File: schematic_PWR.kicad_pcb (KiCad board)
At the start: 2 copper layers, 100 x 100 mm, 116 parts, among them J1 Conn_01x02, J10 Conn_01x02, J11 Conn_01x02, J12 Conn_01x02, J13 Conn_01x02, J14 Conn_01x02, J2 Conn_01x04, J3 Conn_01x04, J4 STlink_v3, J5 Conn_01x02, J6 Conn_01x02, J7 Conn_01x02, J8 Conn_01x02, J9 Conn_01x02, K1 HE1AN-W-DC12V-Y6, Q1 Q_PMOS_GSD, Q2 Q_PMOS_GSD, Q3 Q_PMOS_GSD, Q4 Q_PMOS_GSD, Q5 Q_NMOS_GSD, Q6 Q_NMOS_GSD, Q7 Q_PMOS_GSD, Q8 Q_NMOS_GSD, SW1 SW_SPST, SW2 SW_SPST, SW3 SW_SPST, U1 MCP2562-H-SN, U2 XR76208, U3 STM32F103CBTx, U4 TPS5430DDA, U5 XC6206P332MR-G, Y1 12MHz

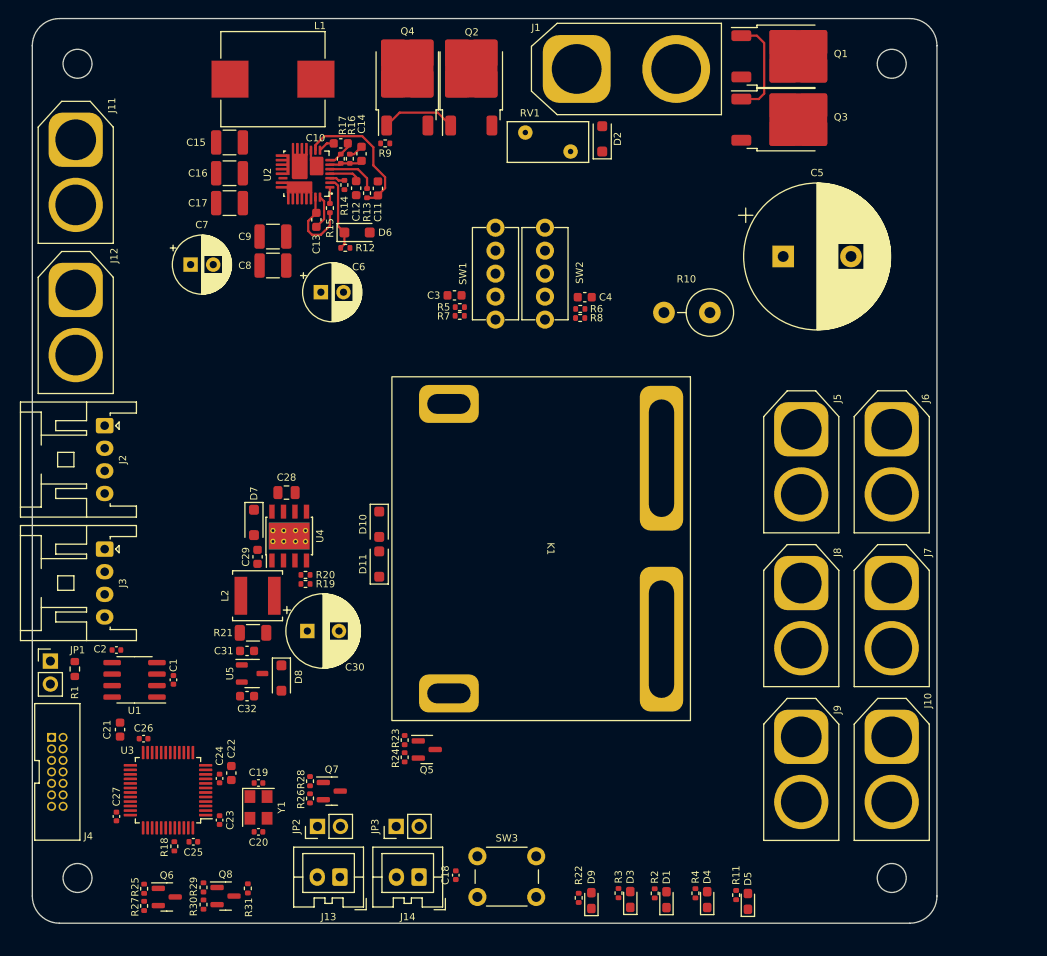
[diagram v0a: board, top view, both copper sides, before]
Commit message: add voltage detector
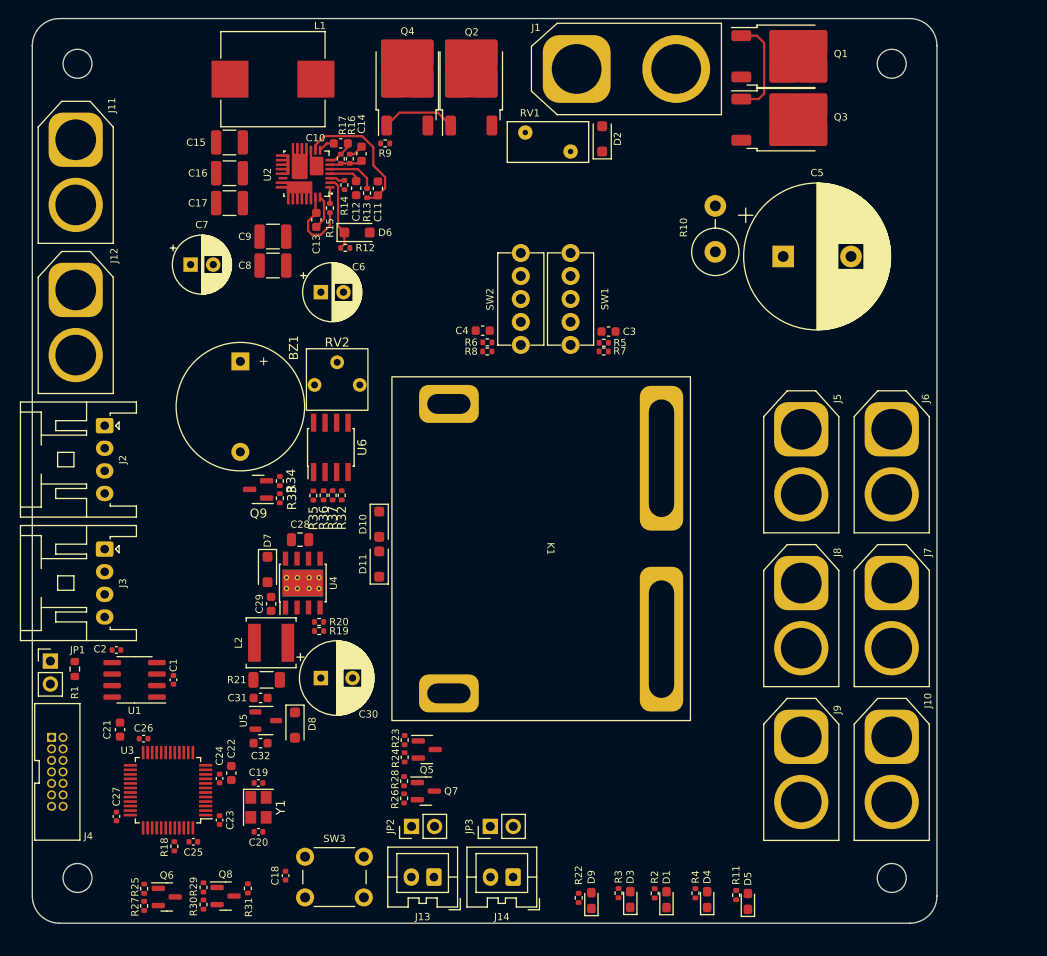
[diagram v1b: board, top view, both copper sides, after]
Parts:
- added BZ1: Buzzer, Buzzer_Beeper:Buzzer_D14mm_H7mm_P10mm, F.Cu at (123.0, 87.9)
- added Q9: Q_NMOS_GSD, Package_TO_SOT_SMD:SOT-23, F.Cu at (125.0, 102.0)
- added R32: R_Small, Resistor_SMD:R_0402_1005Metric, F.Cu at (134.2, 102.7)
- added R33: 100, Resistor_SMD:R_0402_1005Metric, F.Cu at (127.4, 103.0)
- added R34: 10k, Resistor_SMD:R_0402_1005Metric, F.Cu at (127.4, 101.1)
- added R35: 10k, Resistor_SMD:R_0402_1005Metric, F.Cu at (131.1, 102.7)
- added R36: 10k, Resistor_SMD:R_0402_1005Metric, F.Cu at (132.2, 102.7)
- added R37: 20k, Resistor_SMD:R_0402_1005Metric, F.Cu at (133.2, 102.7)
- added RV2: 10k, RDC_generic:GF063P, F.Cu at (133.7, 89.9)
- added U6: LM393, Package_SO:PowerIntegrations_SO-8, F.Cu at (133.0, 97.4)
- C19, C20: value 10pF -> 15pF
- Y1: footprint Crystal:Crystal_SMD_SeikoEpson_FA238V-4Pin_3.2x2.5mm -> Crystal:Crystal_SMD_3225-4Pin_3.2x2.5mm
- moved SW3 19.1 mm to (130.2, 142.7)
- moved C18 18.8 mm to (128.0, 144.7)
- moved C3 17.5 mm to (163.7, 84.6), turned to 180 degrees
- moved R5 16.4 mm to (163.2, 85.8), turned to 180 degrees
- moved R7 16.4 mm to (163.2, 86.8), turned to 0 degrees
- moved C4 11.9 mm to (149.8, 84.5)
- moved R8 10.9 mm to (150.3, 86.8)
- moved R6 10.9 mm to (150.3, 85.8)
- moved J13 10.4 mm to (144.4, 144.9)
- moved J14 10.4 mm to (153.2, 144.9)
- moved JP2 10.4 mm to (141.9, 139.3)
- moved JP3 10.4 mm to (150.6, 139.3)
- moved Q7 10.4 mm to (143.5, 135.4)
- moved R26 10.4 mm to (141.1, 136.2)
- moved R28 10.4 mm to (141.1, 134.3)
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
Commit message: update art work
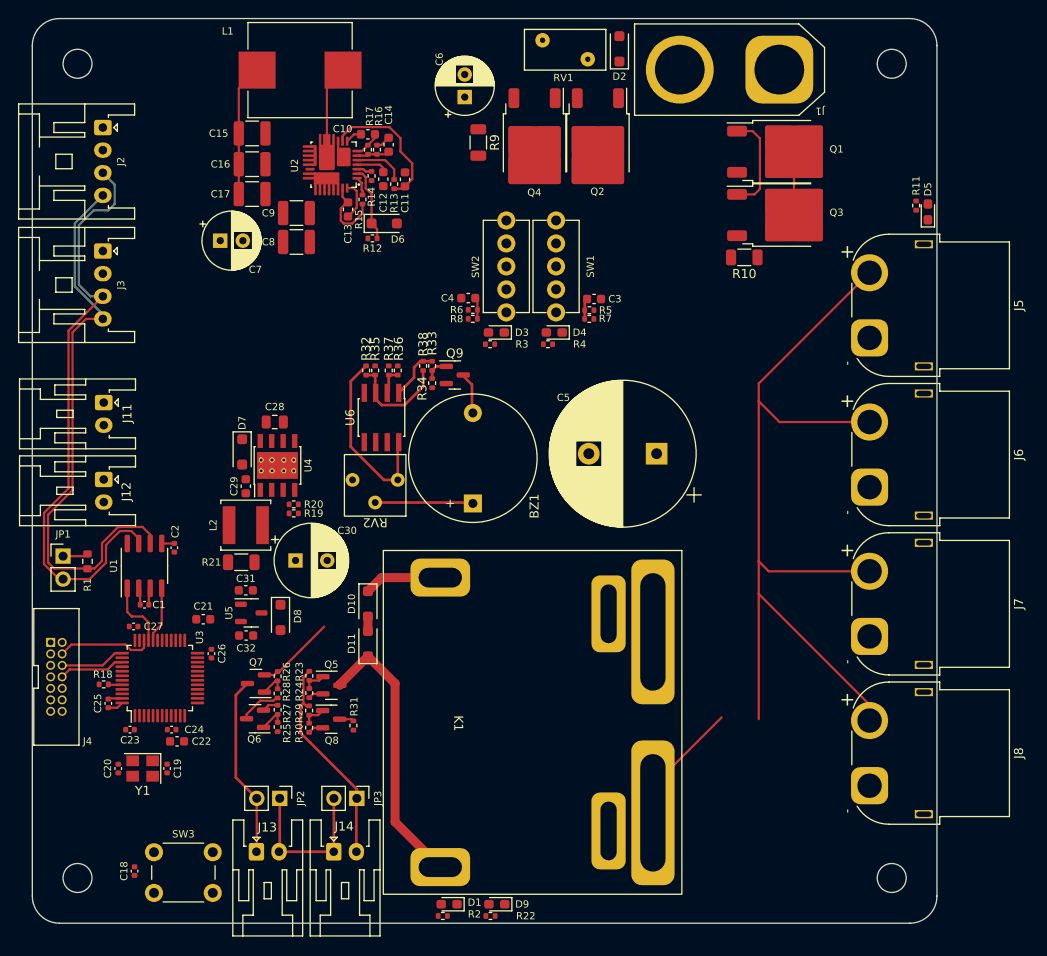
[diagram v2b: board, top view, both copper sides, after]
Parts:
- removed J10, J9: Conn_01x02, Connector_AMASS:AMASS_XT60-F_1x02_P7.20mm_Vertical
- added R38: 15k, Resistor_SMD:R_0402_1005Metric, F.Cu at (143.2, 88.4)
- J11, J12: footprint Connector_AMASS:AMASS_XT60-F_1x02_P7.20mm_Vertical -> Connector_JST:JST_XA_S02B-XASK-1_1x02_P2.50mm_Horizontal
- J13, J14: footprint Connector_JST:JST_XA_B02B-XASK-1_1x02_P2.50mm_Vertical -> Connector_JST:JST_XA_S02B-XASK-1_1x02_P2.50mm_Horizontal
- J5, J6, J7, J8: footprint Connector_AMASS:AMASS_XT60-F_1x02_P7.20mm_Vertical -> Connector_AMASS:AMASS_XT60PW-F_1x02_P7.20mm_Horizontal
- K1: footprint RDC_generic:HE1AN-W-DC12V-Y6 -> RDC_generic:HE1AN-W-DC12V-Y6+Y5
- R10: footprint Resistor_THT:R_Axial_DIN0516_L15.5mm_D5.0mm_P5.08mm_Vertical -> Resistor_SMD:R_1206_3216Metric
- R32: value R_Small -> 2k
- R36: value 10k -> 12K
- R9: footprint Resistor_SMD:R_0402_1005Metric -> Resistor_SMD:R_1206_3216Metric
- moved D5 78.8 mm to (199.0, 71.4)
- moved R11 78.8 mm to (197.7, 70.7)
- moved D4 64.9 mm to (157.7, 84.7), turned to 180 degrees
- moved D3 64.4 mm to (151.3, 84.7), turned to 180 degrees
- moved R4 62.8 mm to (157.0, 86.0), turned to 180 degrees
- moved R3 62.3 mm to (150.6, 86.0), turned to 180 degrees
- moved J2 33.0 mm to (107.8, 62.0)
- moved J3 33.0 mm to (107.8, 75.7)
- moved BZ1 30.1 mm to (148.7, 103.6), turned to 90 degrees
- moved J11 29.2 mm to (107.9, 92.5)
- moved C6 26.8 mm to (147.8, 58.7), turned to 90 degrees
- moved R27 26.2 mm to (127.1, 126.4), turned to 90 degrees
- moved C5 25.9 mm to (169.0, 98.1), turned to 180 degrees
- moved Q9 25.2 mm to (146.7, 89.4), turned to 0 degrees
- moved D1 24.0 mm to (146.1, 147.9), turned to 180 degrees
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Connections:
- Q9 pad 2: /Voltage_detector/GND -> GND
- R32 pad 1: /Voltage_detector/V+ -> +12V
- R32 pad 2: Net-(D12-K) -> Net-(U6A-+)
- R34 pad 1: Net-(Q9-G) -> GND
- R34 pad 2: /Voltage_detector/GND -> Net-(Q9-G)
- R35 pad 1: /Voltage_detector/Vcc -> Net-(U6A-+)
- R35 pad 2: Net-(R33-Pad2) -> GND
- R36 pad 1: /Voltage_detector/V- -> Logic_line_Power
- R37 pad 2: /Voltage_detector/GND -> GND
- RV2 pad 1: /Voltage_detector/Vcc -> +12V
- RV2 pad 3: /Voltage_detector/GND -> GND
- U6 pad 3: Net-(D12-K) -> Net-(U6A-+)
- U6 pad 4: /Voltage_detector/GND -> GND
- U6 pad 8: /Voltage_detector/Vcc -> +12V
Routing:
- net /Power_relay/Main_power_OUT: track 0.00 -> 109.4 mm
- net Net-(J2-Pin_3): track 0.00 -> 66.4 mm
- net Net-(J2-Pin_4): track 0.00 -> 62.7 mm
- net +12V: track 1.63 -> 54.3 mm
- net Net-(D11-K): track 0.00 -> 31.9 mm
- net /EMS/Relay_Signal_OUT: track 0.00 -> 23.7 mm
- net Net-(J13-Pin_1): track 0.00 -> 20.2 mm
- net Net-(J13-Pin_2): track 0.00 -> 17.9 mm
- net Net-(U6A-+): track 0.00 -> 11.8 mm
- net Net-(BZ1--): track 0.00 -> 10.7 mm
- net /STM32F103/SWDIO: track 0.00 -> 10.6 mm
- net Net-(C13-Pad1): track 8.50 -> 18.5 mm
- net GND: track 0.00 -> 8.63 mm
- net /STM32F103/CAN_TX: track 0.00 -> 7.44 mm
- net /STM32F103/SWO: track 0.00 -> 7.31 mm
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
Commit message: アートワークのほとんど終わり
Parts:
- removed C2: 0.1uF, Capacitor_SMD:C_0402_1005Metric
- added R39: 10k, Resistor_SMD:R_1206_3216Metric, F.Cu at (122.5, 83.5)
- D1: footprint LED_SMD:LED_0603_1608Metric_Pad1.05x0.95mm_HandSolder -> LED_SMD:LED_0805_2012Metric
- D10: value D_Schottky -> D
- D11: footprint Diode_SMD:D_SOD-123F -> Diode_SMD:D_SMA
- D2: value D -> D_Schottky
- D3, D4, D5, D9: footprint LED_SMD:LED_0603_1608Metric_Pad1.05x0.95mm_HandSolder -> LED_SMD:LED_0603_1608Metric
- D6: footprint Diode_SMD:D_SOD-123F -> Diode_SMD:D_SOD-123
- L1: value 8.2u -> 8.2uH
- R16: value 38k -> 47k
- R17, R32: value 2k -> 2.4k
- R2: value 10k -> 1.2k
- R36: value 12K -> 12k
- SW3: footprint Button_Switch_THT:SW_PUSH_6mm_H7.3mm -> RDC_generic:TVBP06-B043
- U1: value MCP2562-H-SN -> SN65HVD230
- moved D1 34.7 mm to (111.4, 145.7)
- moved R2 34.7 mm to (110.7, 147.3), turned to 0 degrees
- moved R22 34.0 mm to (116.7, 147.3), turned to 0 degrees
- moved D9 34.0 mm to (117.4, 146.0)
- moved C4 27.6 mm to (165.4, 59.3), turned to -90 degrees
- moved R8 26.7 mm to (164.6, 61.8), turned to -90 degrees
- moved R6 26.5 mm to (165.6, 61.8), turned to 90 degrees
- moved R5 21.4 mm to (178.6, 69.2), turned to -90 degrees
- moved R7 20.6 mm to (177.1, 69.7), turned to 180 degrees
- moved C3 19.1 mm to (176.6, 68.5), turned to 0 degrees
- moved R31 15.4 mm to (133.3, 112.9), turned to 0 degrees
- moved SW3 13.4 mm to (104.0, 132.7), turned to -90 degrees
- moved Q8 12.3 mm to (132.4, 115.1)
- moved R29 12.3 mm to (129.9, 114.2)
- moved R30 12.3 mm to (129.9, 116.1)
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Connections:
- C1 pad 2: +5V -> +3.3V
- C10 pad 2: /Stepdown_12V_8A/GND -> GND
- C11 pad 2: /Stepdown_12V_8A/GND -> GND
- C12 pad 2: /Stepdown_12V_8A/GND -> GND
- C15 pad 2: /Stepdown_12V_8A/GND -> GND
- C16 pad 2: /Stepdown_12V_8A/GND -> GND
- C17 pad 2: /Stepdown_12V_8A/GND -> GND
- C8 pad 2: /Stepdown_12V_8A/GND -> GND
- C9 pad 2: /Stepdown_12V_8A/GND -> GND
- D6 pad 2: /Stepdown_12V_8A/GND -> GND
- R14 pad 2: /Stepdown_12V_8A/GND -> GND
- R17 pad 2: /Stepdown_12V_8A/GND -> GND
- U1 pad 3: +5V -> +3.3V
- U1 pad 5: +3.3V -> unconnected-(U1-Vref-Pad5)
- U2 pad 10: /Stepdown_12V_8A/GND -> GND
- U2 pad 15: /Stepdown_12V_8A/GND -> GND
- U2 pad 16: /Stepdown_12V_8A/GND -> GND
- U2 pad 17: /Stepdown_12V_8A/GND -> GND
- U2 pad 18: /Stepdown_12V_8A/GND -> GND
- U2 pad 19: /Stepdown_12V_8A/GND -> GND
- U2 pad 20: Net-(C13-Pad1) -> unconnected-(U2-SW-Pad20)
- U2 pad 7: /Stepdown_12V_8A/GND -> GND
- U2 pad AGND: /Stepdown_12V_8A/GND -> GND
- U2 pad PGND: /Stepdown_12V_8A/GND -> GND
- U3 pad 17: unconnected-(U3-PA7-Pad17) -> MCU_running
- U3 pad 18: unconnected-(U3-PB0-Pad18) -> /EMS/MCU_EMC_signal
- U3 pad 19: unconnected-(U3-PB1-Pad19) -> /EMS/MCU_EMS_Observe
- U3 pad 40: /EMS/MCU_EMC_signal -> unconnected-(U3-PB4-Pad40)
- U3 pad 41: /EMS/MCU_EMS_Observe -> unconnected-(U3-PB5-Pad41)
- U3 pad 42: MCU_running -> unconnected-(U3-PB6-Pad42)
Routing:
- net +12V: track 54.3 -> 162.7 mm, vias 0 -> 5
- net /Power_relay/Main_power_OUT: track 109.4 -> 7.51 mm
- net +3.3V: track 3.15 -> 97.2 mm, vias 0 -> 8
- net GND: track 8.63 -> 82.1 mm, vias 0 -> 75
- net MCU_running: track 0.00 -> 31.7 mm, vias 0 -> 2
- net Net-(D11-K): track 31.9 -> 58.8 mm
- net Logic_line_Power: track 1.84 -> 26.6 mm, vias 0 -> 2
- net Net-(SW1-B): track 0.00 -> 24.6 mm
- net +5V: track 1.89 -> 25.5 mm, vias 0 -> 1
- net Net-(SW2-B): track 0.00 -> 22.5 mm
- net Net-(SW3-B): track 0.00 -> 21.2 mm, vias 0 -> 2
- net /EMS/MCU_EMS_Observe: track 1.60 -> 21.2 mm, vias 0 -> 4
- net Net-(Q2-G): track 2.40 -> 15.4 mm
- net /EMS/MCU_EMC_signal: track 0.00 -> 12.4 mm, vias 0 -> 4
- net Net-(U3-PD0): track 0.00 -> 9.58 mm
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- added copper zone on F.Cu, net +12V
- added copper zone on F.Cu, net +5V
- added copper zone on F.Cu, net +BATT
- added copper zone on F.Cu, net /Power_relay/Main_power_OUT
- added copper zone on F.Cu, net Actuator_Power
- added copper zone on B.Cu, net GND
- added copper zone on F.Cu, net GND
- added copper zone on F.Cu, net Logic_line_Power
- added copper zone on F.Cu, net Net-(C13-Pad1)
- added copper zone on F.Cu, net Net-(D7-K)
- added copper zone on F.Cu, net Net-(Q1-D)
- added copper zone on F.Cu, net Net-(Q2-D)
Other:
- board text added: "12V"
- board text added: "14.4V以下"
- board text added: "CAN"
- board text added: "OFF"
- board text added: "ON"
- board text added: "Operation"
- board text added: "RESET"
- board text added: "STlink"
- board text added: "バッテリー"
- board text added: "制御電源"
- board text added: "終端抵抗"
- board text added: "電圧低下検知"
- board text added: "非常停止ボタン"
- board text added: "音量調整"
- board text added: "駆動系電源"
- board text added: "駆動電源"
